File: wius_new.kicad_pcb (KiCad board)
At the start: 6 copper layers, 54 x 28 mm, 114 parts, among them IC1 BQ24040DSQT, J2 52746-1271, J3 1040310811, J4 SS5-10-3.00-L-D-K-TR, J5 USB4745-03-A, J8 2, J9 U.FL, M1 MountingHole_Pad, M2 MountingHole_Pad, M3 MountingHole_Pad, M4 MountingHole_Pad, SW3 Button Switch SPST-No, SW4 Button Switch SPST-No, U1 TPS62840YBGR, U12 SN74LVC1T45DCK, U13 TXB0104RUT, U2 TXB0104RUT, U3 SiWG917Y, U4 FT232HPQ, U5 LSM6DSV, U6 SN74AXC4T774RSVR, U8 TXB0104RUT, U9 PCAL6408AHK, Y1 SIT1552AI-JE-DCC-32.768E

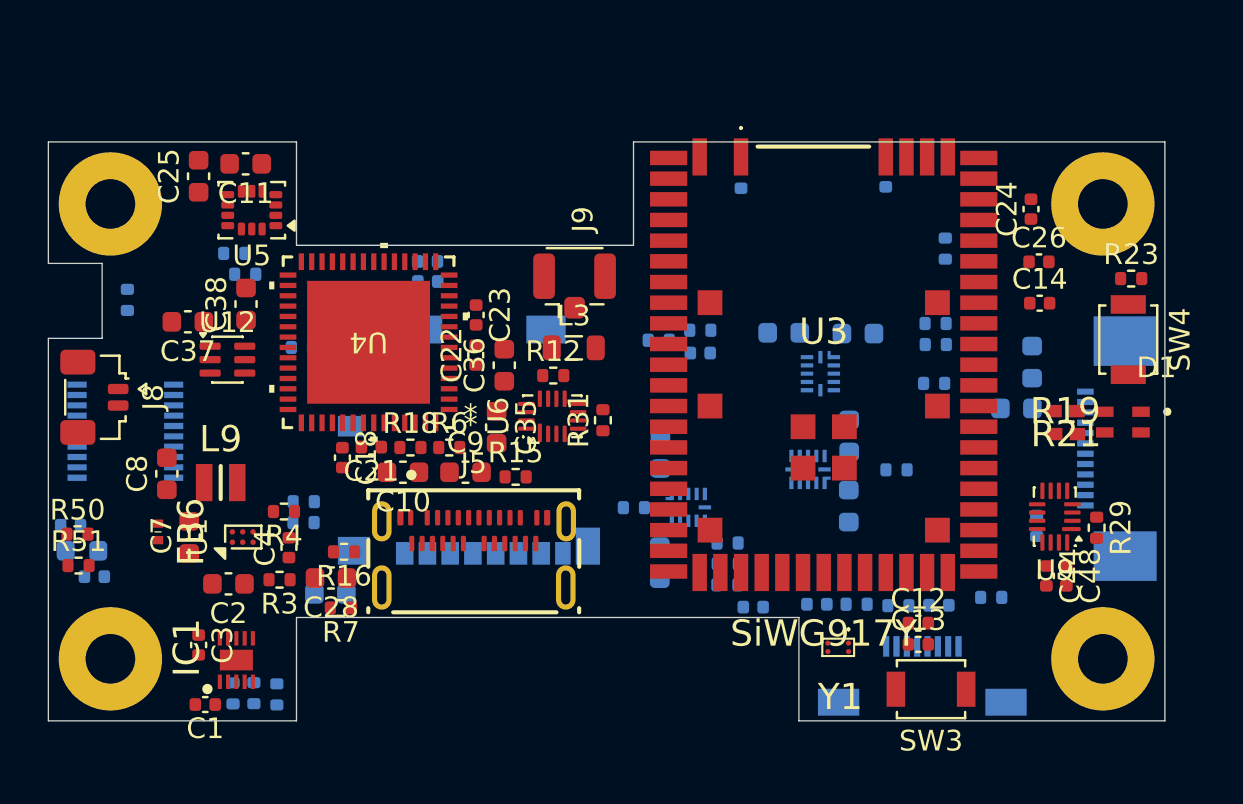
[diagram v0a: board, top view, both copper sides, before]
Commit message: new debug connector SOICbite, new board shape, new placement, addition of 22 ohm resistance in fast digital signals as spi
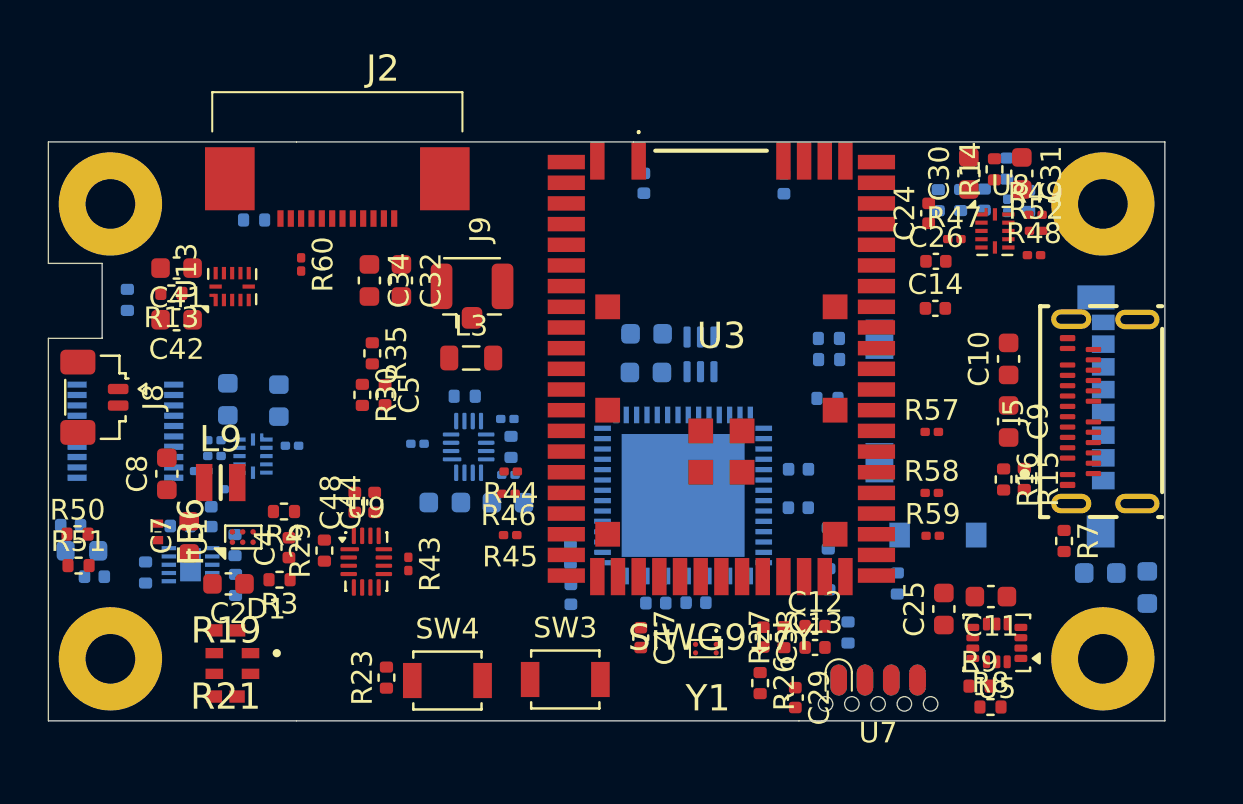
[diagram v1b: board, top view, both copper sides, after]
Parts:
- removed PJ2: 5051100892, dz_con:CON_5051100892_MOL
- removed R28: 22, Resistor_SMD:R_0402_1005Metric
- added R36: 22, Resistor_SMD:R_0201_0603Metric, B.Cu at (131.0, 100.4)
- added R37: 22, Resistor_SMD:R_0201_0603Metric, B.Cu at (131.8, 102.8)
- added R41: 22, Resistor_SMD:R_0201_0603Metric, B.Cu at (130.4, 101.9)
- added R42: 22, Resistor_SMD:R_0201_0603Metric, B.Cu at (134.8, 100.7)
- added R43: 22, Resistor_SMD:R_0201_0603Metric, F.Cu at (140.4, 106.4)
- added R44: 22, Resistor_SMD:R_0201_0603Metric, F.Cu at (145.4, 101.9)
- added R45: 22, Resistor_SMD:R_0201_0603Metric, F.Cu at (145.3, 105.0)
- added R46: 22, Resistor_SMD:R_0201_0603Metric, F.Cu at (145.3, 103.0)
- added R47: 22, Resistor_SMD:R_0201_0603Metric, F.Cu at (166.8, 90.7)
- added R48: 22, Resistor_SMD:R_0201_0603Metric, F.Cu at (170.7, 91.5)
- added R49: 22, Resistor_SMD:R_0201_0603Metric, F.Cu at (170.7, 89.5)
- added R5: 22, Resistor_SMD:R_0201_0603Metric, B.Cu at (131.0, 101.2)
- added R52: 22, Resistor_SMD:R_0201_0603Metric, F.Cu at (170.8, 90.3)
- added R53: 22, Resistor_SMD:R_0201_0603Metric, B.Cu at (169.4, 89.1)
- added R54: 22, Resistor_SMD:R_0201_0603Metric, B.Cu at (140.8, 100.6)
- added R55: 22, Resistor_SMD:R_0201_0603Metric, B.Cu at (145.2, 102.1)
- added R56: 22, Resistor_SMD:R_0201_0603Metric, B.Cu at (145.2, 99.4)
- added R57: 22, Resistor_SMD:R_0201_0603Metric, F.Cu at (165.7, 100.0)
- added R58: 22, Resistor_SMD:R_0201_0603Metric, F.Cu at (165.7, 103.0)
- added R59: 22, Resistor_SMD:R_0201_0603Metric, F.Cu at (165.8, 105.0)
- added R60: 22, Resistor_SMD:R_0201_0603Metric, F.Cu at (135.2, 91.9)
- added U7: SOIC_clipProgSmall, dz_mech:SOIC_clipProgSmall, F.Cu at (163.1, 112.5)
- C1, C18, C21, C22, C23, C28, C3, C35, C36, C37, C38, IC1, R12, R18, R31, R6, U12, U4, U6: moved to B.Cu
- C29, C30, C31, C32, C33, C34, C41, C42, C47, C5, J2, R13, R14, R26, R27, R30, R35, R8, R9, U13, U8: moved to F.Cu
- moved D1 44.6 mm to (131.9, 111.2)
- moved R21 42.6 mm to (131.6, 112.8), turned to 180 degrees
- moved R19 42.0 mm to (131.6, 109.6), turned to 180 degrees
- moved J2 41.7 mm to (137.0, 86.7), turned to 180 degrees
- moved C25 41.7 mm to (166.3, 108.6)
- moved C11 41.7 mm to (168.6, 108.0)
- moved R8 41.7 mm to (168.6, 113.3)
- moved R9 41.7 mm to (168.0, 112.3)
- moved U5 41.7 mm to (168.9, 110.2)
- moved R23 40.9 mm to (139.3, 111.9), turned to 90 degrees
- moved R20 40.6 mm to (132.9, 89.8), turned to 0 degrees
- moved C27 39.5 mm to (176.2, 107.5), turned to -90 degrees
- moved R11 38.0 mm to (170.4, 88.8), turned to -90 degrees
- moved R29 37.4 mm to (136.3, 105.8), turned to 90 degrees
- moved C28 37.2 mm to (173.9, 106.8)
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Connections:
- J2 pad 10: /MCU/ULP_SSI.MISO -> Net-(J2-Pad10)
- J3 pad 7: /IMU_SD/SPI_SD.MISO -> Net-(J3-DAT0)
- J4 pad 4: /connectors/FPGA_MISO -> Net-(J4-Pad4)
- U2 pad 10: /connectors/FPGA_MISO -> Net-(U2-B1)
- U2 pad 2: /MCU/SPI_FPGA.MISO -> /MCU/SPI_FPGA.MOSI
- U2 pad 4: /MCU/SPI_FPGA.CS0 -> Net-(U2-A3)
- U2 pad 5: /MCU/SPI_FPGA.MOSI -> /MCU/SPI_FPGA.CS0
- U2 pad 7: /connectors/FPGA_MOSI -> Net-(U2-B4)
- U2 pad 8: /connectors/FPGA_CS -> /connectors/FPGA_MISO
- U2 pad 9: /connectors/FPGA_SCLK -> Net-(U2-B2)
- U3 pad 18: /IMU_SD/SPI_MCU.CS0 -> Net-(U3C-GPIO_53)
- U3 pad 19: /IMU_SD/SPI_MCU.CS1 -> Net-(U3C-GPIO_54)
- U3 pad 21: /IMU_SD/SPI_MCU.MOSI -> Net-(U3C-GPIO_57)
- U3 pad 25: /IMU_SD/SPI_MCU.SCK -> Net-(U3C-GPIO_52)
- U3 pad 39: /MCU/ULP_SSI.CS0 -> Net-(U3C-GPIO_48)
- U3 pad 41: /MCU/ULP_SSI.MOSI -> Net-(U3C-GPIO_49)
- U3 pad 44: /MCU/ULP_SSI.SCK -> Net-(U3C-GPIO_46)
- U3 pad 53: Net-(U3C-GPIO_26) -> /MCU/SPI_FPGA.MISO
- U6 pad 12: /USB_FT232HPQ/SPI_FT232.SCK -> Net-(U6-B1)
- U6 pad 3: /IMU_SD/SPI_MCU.MISO -> Net-(U6-A3)
- U6 pad 9: /USB_FT232HPQ/SPI_FT232.CS -> Net-(U6-B4)
- U8 pad 10: /IMU_SD/SPI_SD.SCK -> Net-(U8-B1)
- U8 pad 4: /IMU_SD/SPI_MCU.MISO -> Net-(U8-A3)
- U8 pad 7: /IMU_SD/SPI_SD.CS0 -> Net-(U8-B4)
- U8 pad 9: /IMU_SD/SPI_SD.MOSI -> Net-(U8-B2)
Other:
- outline, holes or cut-outs redrawn
